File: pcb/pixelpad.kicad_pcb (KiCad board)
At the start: 2 copper layers, 16 parts, among them J1 OLED Display, SW1 SW_Push_45deg, SW2 SW_Push_45deg, SW3 RotaryEncoder_Switch, SW4 SW_Push_45deg, SW5 SW_Push_45deg, SW6 SW_Push_45deg, U1 MOUDLE-SEEEDUINO-XIAO

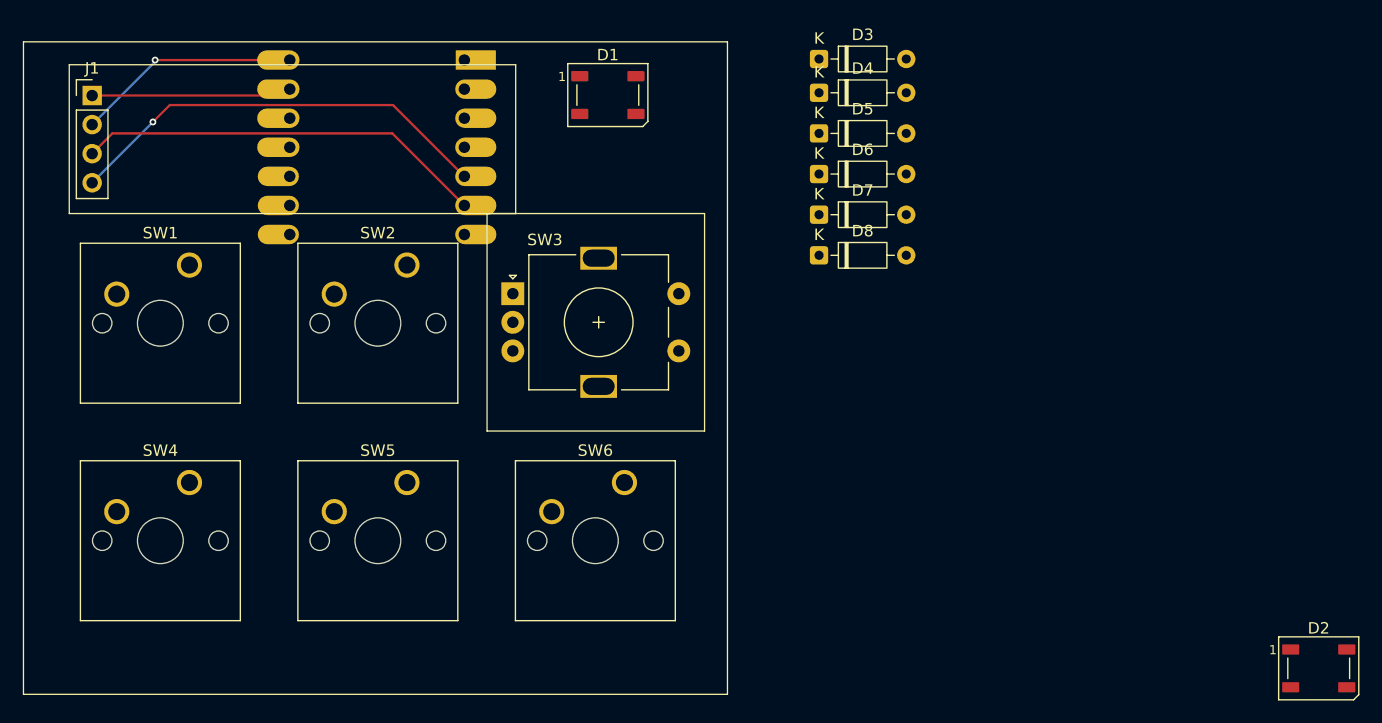
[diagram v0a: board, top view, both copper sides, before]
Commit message: Reordering pins so it's easier to route
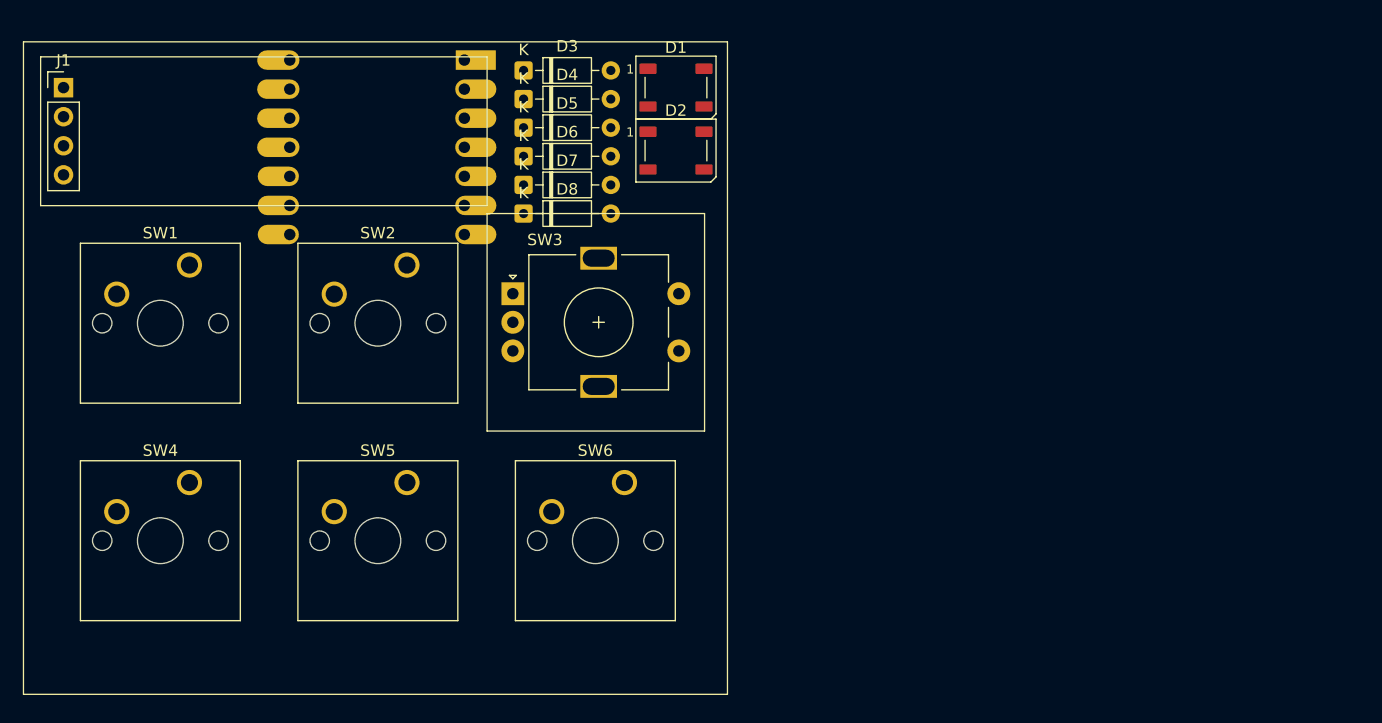
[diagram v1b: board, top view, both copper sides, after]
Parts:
- moved D2 72.1 mm to (112.5, 44.0)
- moved D8 26.1 mm to (99.2, 49.5)
- moved D7 25.9 mm to (99.2, 47.0)
- moved D6 25.9 mm to (99.2, 44.5)
- moved D3 25.8 mm to (99.2, 37.0)
- moved D4 25.8 mm to (99.2, 39.5)
- moved D5 25.8 mm to (99.2, 42.0)
- moved D1 5.99 mm to (112.5, 38.5)
- moved J1 2.59 mm to (59.0, 38.5)
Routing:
- net SDA: track 37.9 -> 0.00 mm, vias 1 -> 0
- net SCL: track 35.9 -> 0.00 mm
- net VCC: track 19.7 -> 0.00 mm, vias 1 -> 0
- net GND: track 17.5 -> 0.00 mm
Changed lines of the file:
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@@
 	(footprint "LED_SMD:LED_WS2812B_PLCC4_5.0x5.0mm_P3.2mm"
 		(layer "F.Cu")
-		(at 168.65 89.23)
+		(at 112.5 44)
 		(descr "5.0mm x 5.0mm Addressable RGB LED NeoPixel, https://cdn-shop.adafruit.com/datasheets/WS2812B.pdf")
 		(tags "LED RGB NeoPixel PLCC-4 5050")
@@
 	(footprint "Diode_THT:D_DO-35_SOD27_P7.62mm_Horizontal"
 		(layer "F.Cu")
-		(at 125 38.95)
+		(at 99.19 39.5)
 		(descr "Diode, DO-35_SOD27 series, Axial, Horizontal, pin pitch=7.62mm, length*diameter=4*2mm^2, http://www.diodes.com/_files/packages/DO-35.pdf")
 		(tags "Diode DO-35_SOD27 series Axial Horizontal pin pitch 7.62mm  length 4mm diameter 2mm")
@@
 		)
 		(property "Value" "1N914"
-			(at 3.81 2.12 0)
+			(at 3.81 -2.53 0)
 			(layer "F.Fab")
 			(effects
@@
 	(footprint "Diode_THT:D_DO-35_SOD27_P7.62mm_Horizontal"
 		(layer "F.Cu")
-		(at 125 46.05)
+		(at 99.19 44.5)
 		(descr "Diode, DO-35_SOD27 series, Axial, Horizontal, pin pitch=7.62mm, length*diameter=4*2mm^2, http://www.diodes.com/_files/packages/DO-35.pdf")
 		(tags "Diode DO-35_SOD27 series Axial Horizontal pin pitch 7.62mm  length 4mm diameter 2mm")
@@
 	(footprint "LED_SMD:LED_WS2812B_PLCC4_5.0x5.0mm_P3.2mm"
 		(layer "F.Cu")
-		(at 106.55 39.15)
+		(at 112.5 38.5)
 		(descr "5.0mm x 5.0mm Addressable RGB LED NeoPixel, https://cdn-shop.adafruit.com/datasheets/WS2812B.pdf")
 		(tags "LED RGB NeoPixel PLCC-4 5050")
@@
 	(footprint "Diode_THT:D_DO-35_SOD27_P7.62mm_Horizontal"
 		(layer "F.Cu")
-		(at 125 42.5)
+		(at 99.19 42)
 		(descr "Diode, DO-35_SOD27 series, Axial, Horizontal, pin pitch=7.62mm, length*diameter=4*2mm^2, http://www.diodes.com/_files/packages/DO-35.pdf")
 		(tags "Diode DO-35_SOD27 series Axial Horizontal pin pitch 7.62mm  length 4mm diameter 2mm")
@@
 	(footprint "Connector_PinHeader_2.54mm:PinHeader_1x04_P2.54mm_Vertical"
 		(layer "F.Cu")
-		(at 61.5 39.19)
+		(at 59 38.5)
 		(descr "Through hole straight pin header, 1x04, 2.54mm pitch, single row")
 		(tags "Through hole pin header THT 1x04 2.54mm single row")
@@
 	(footprint "Diode_THT:D_DO-35_SOD27_P7.62mm_Horizontal"
 		(layer "F.Cu")
-		(at 125 49.6)
+		(at 99.19 47)
 		(descr "Diode, DO-35_SOD27 series, Axial, Horizontal, pin pitch=7.62mm, length*diameter=4*2mm^2, http://www.diodes.com/_files/packages/DO-35.pdf")
 		(tags "Diode DO-35_SOD27 series Axial Horizontal pin pitch 7.62mm  length 4mm diameter 2mm")
@@
 	(footprint "Diode_THT:D_DO-35_SOD27_P7.62mm_Horizontal"
 		(layer "F.Cu")
-		(at 125 36)
+		(at 99.19 37)
 		(descr "Diode, DO-35_SOD27 series, Axial, Horizontal, pin pitch=7.62mm, length*diameter=4*2mm^2, http://www.diodes.com/_files/packages/DO-35.pdf")
 		(tags "Diode DO-35_SOD27 series Axial Horizontal pin pitch 7.62mm  length 4mm diameter 2mm")
@@
 	(footprint "Diode_THT:D_DO-35_SOD27_P7.62mm_Horizontal"
 		(layer "F.Cu")
-		(at 125 53.15)
+		(at 99.19 49.5)
 		(descr "Diode, DO-35_SOD27 series, Axial, Horizontal, pin pitch=7.62mm, length*diameter=4*2mm^2, http://www.diodes.com/_files/packages/DO-35.pdf")
 		(tags "Diode DO-35_SOD27 series Axial Horizontal pin pitch 7.62mm  length 4mm diameter 2mm")
@@
 	)
 	(gr_rect
-		(start 59.5 36.5)
-		(end 98.5 49.5)
+		(start 57 35.81)
+		(end 96 48.81)
 		(stroke
 			(width 0.1)
@@
 		(layer "F.SilkS")
 	)
-	(segment
-		(start 67 36.092015)
-		(end 78.7645 36.092015)
-		(width 0.2)
-		(layer "F.Cu")
-		(net "VCC")
-	)
-	(via
-		(at 67 36.092015)
-		(size 0.6)
-		(drill 0.3)
-		(layers "F.Cu" "B.Cu")
-		(net "VCC")
-	)
-	(segment
-		(start 67 36.23)
-		(end 61.5 41.73)
-		(width 0.2)
-		(layer "B.Cu")
-		(net "VCC")
-	)
-	(segment
-		(start 67 36.092015)
-		(end 67 36.23)
-		(width 0.2)
-		(layer "B.Cu")
-		(net "VCC")
-	)
-	(segment
-		(start 78.206515 39.19)
-		(end 78.7645 38.632015)
-		(width 0.2)
-		(layer "F.Cu")
-		(net "GND")
-	)
-	(segment
-		(start 61.5 39.19)
-		(end 78.206515 39.19)
-		(width 0.2)
-		(layer "F.Cu")
-		(net "GND")
-	)
-	(segment
-		(start 63.27 42.5)
-		(end 61.5 44.27)
-		(width 0.2)
-		(layer "F.Cu")
-		(net "SCL")
-	)
-	(segment
-		(start 87.722485 42.5)
-		(end 63.27 42.5)
-		(width 0.2)
-		(layer "F.Cu")
-		(net "SCL")
-	)
-	(segment
-		(start 94.0145 48.792015)
-		(end 87.722485 42.5)
-		(width 0.2)
-		(layer "F.Cu")
-		(net "SCL")
-	)
-	(segment
-		(start 66.81 41.5)
-		(end 68.287985 40.022015)
-		(width 0.2)
-		(layer "F.Cu")
-		(net "SDA")
-	)
-	(segment
-		(start 68.287985 40.022015)
-		(end 87.7845 40.022015)
-		(width 0.2)
-		(layer "F.Cu")
-		(net "SDA")
-	)
-	(segment
-		(start 87.7845 40.022015)
-		(end 94.0145 46.252015)
-		(width 0.2)
-		(layer "F.Cu")
-		(net "SDA")
-	)
-	(via
-		(at 66.81 41.5)
-		(size 0.6)
-		(drill 0.3)
-		(layers "F.Cu" "B.Cu")
-		(net "SDA")
-	)
-	(segment
-		(start 66.81 41.5)
-		(end 61.5 46.81)
-		(width 0.2)
-		(layer "B.Cu")
-		(net "SDA")
-	)
 	(group ""

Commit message: Ran DRC and no more errors
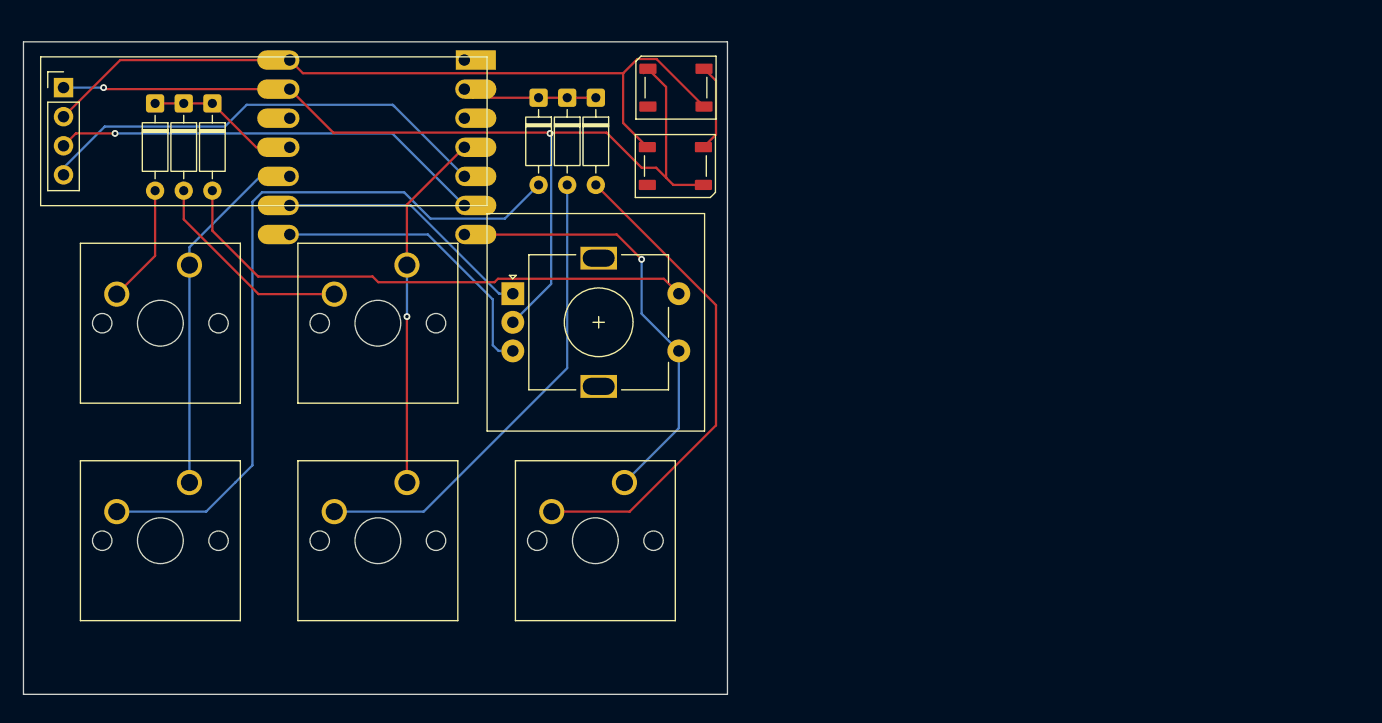
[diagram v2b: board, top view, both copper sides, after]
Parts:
- moved D3 32.3 mm to (67.0, 39.9), turned to -90 degrees
- moved D4 29.7 mm to (69.5, 39.9), turned to -90 degrees
- moved D5 27.3 mm to (72.0, 39.9), turned to -90 degrees
- moved D8 11.9 mm to (105.5, 39.4), turned to -90 degrees
- moved D7 8.52 mm to (103.0, 39.4), turned to -90 degrees
- moved D6 5.28 mm to (100.5, 39.4), turned to -90 degrees
- moved D2 1.35 mm to (112.5, 45.4)
- turned D1 to 180 degrees
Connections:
- U1 pad 1: COL0 -> unconnected-(U1-PA02_A0_D0-Pad1)
- U1 pad 10: COL2 -> COL0
- U1 pad 11: COL1 -> ROW0
- U1 pad 2: unconnected-(U1-PA4_A1_D1-Pad2) -> ROW1
- U1 pad 3: ROW1 -> unconnected-(U1-PA10_A2_D2-Pad3)
- U1 pad 4: ROW0 -> COL1
- U1 pad 7: unconnected-(U1-PB08_A6_D6_TX-Pad7) -> COL2
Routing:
- net GND: track 0.00 -> 88.2 mm, vias 0 -> 2
- net VCC: track 0.00 -> 68.0 mm
- net Net-(D6-A): track 0.00 -> 64.1 mm
- net EC11SWA: track 0.00 -> 46.8 mm
- net Net-(D8-A): track 0.00 -> 42.8 mm
- net Net-(D7-A): track 0.00 -> 41.5 mm
- net SDA: track 0.00 -> 40.6 mm
- net COL2: track 0.00 -> 39.2 mm, vias 0 -> 1
- net SCL: track 0.00 -> 38.1 mm, vias 0 -> 1
- net COL0: track 0.00 -> 31.9 mm
- net COL1: track 0.00 -> 31.4 mm, vias 0 -> 1
- net EC11B: track 0.00 -> 26.0 mm
- net EC11A: track 0.00 -> 22.7 mm
- net Net-(D4-A): track 0.00 -> 18.4 mm
- net ROW0: track 0.00 -> 13.4 mm
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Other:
- board outline added: 61.5 x 57 mm

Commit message: Trying to add custom silkscreen
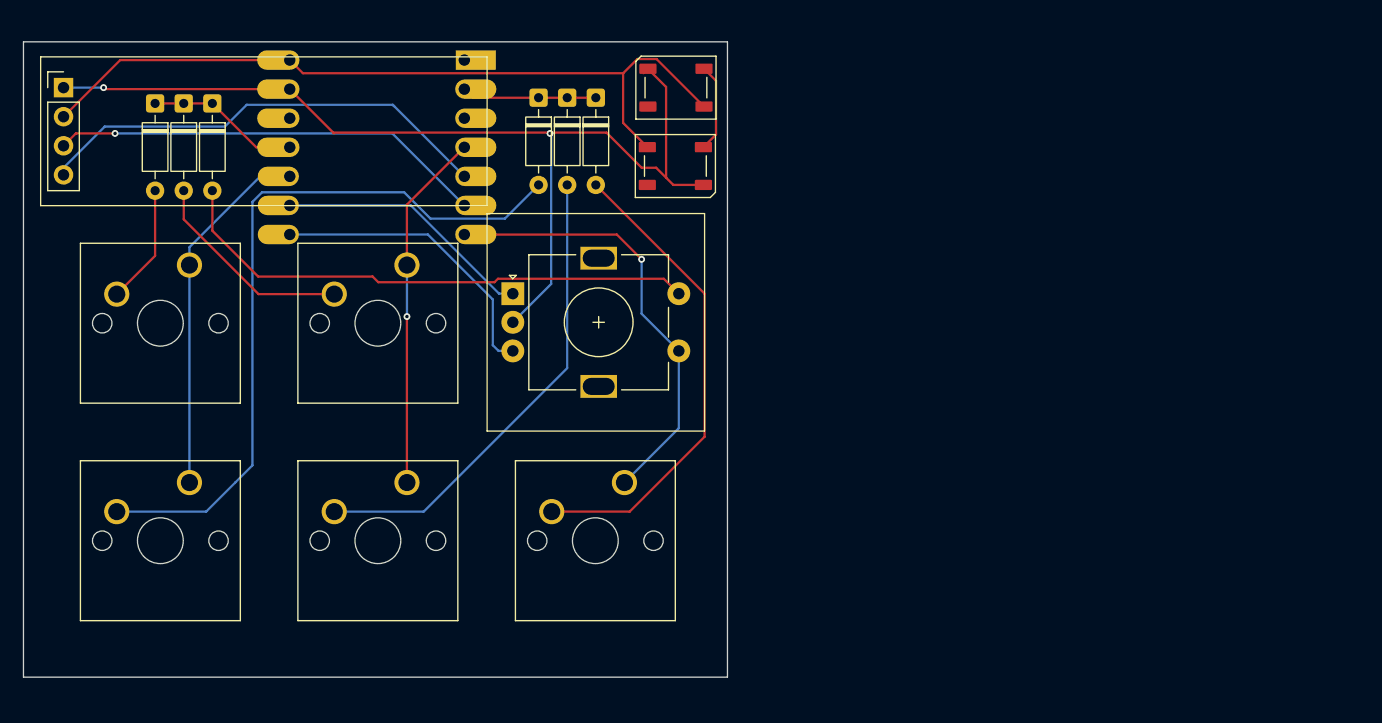
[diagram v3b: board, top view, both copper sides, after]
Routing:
- net Net-(D8-A): track 42.8 -> 42.0 mm
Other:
- board size 61.5 x 57 mm -> 61.5 x 55.5 mm
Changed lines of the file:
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@@
 	(gr_rect
 		(start 55.5 34.5)
-		(end 117 91.5)
+		(end 117 90)
 		(stroke
 			(width 0.05)
@@
 	)
 	(segment
-		(start 116 57.5)
-		(end 116 68)
+		(start 105.5 47)
+		(end 115 56.5)
+		(width 0.2)
+		(layer "F.Cu")
+		(net "Net-(D8-A)")
+	)
+	(segment
+		(start 115 69)
+		(end 108.46 75.54)
+		(width 0.2)
+		(layer "F.Cu")
+		(net "Net-(D8-A)")
+	)
+	(segment
+		(start 115 56.5)
+		(end 115 69)
 		(width 0.2)
 		(layer "F.Cu")
@@
 	)
 	(segment
-		(start 105.5 47)
-		(end 116 57.5)
-		(width 0.2)
-		(layer "F.Cu")
-		(net "Net-(D8-A)")
-	)
-	(segment
-		(start 116 68)
-		(end 108.46 75.54)
-		(width 0.2)
-		(layer "F.Cu")
-		(net "Net-(D8-A)")
+		(start 89.342015 48.792015)
+		(end 97.05 56.5)
+		(width 0.2)
+		(layer "B.Cu")
+		(net "EC11A")
+	)
+	(segment
+		(start 78.7645 48.792015)
+		(end 89.342015 48.792015)
+		(width 0.2)
+		(layer "B.Cu")
+		(net "EC11A")
+	)
+	(segment
+		(start 97.05 56.5)
+		(end 98.25 56.5)
+		(width 0.2)
+		(layer "B.Cu")
+		(net "EC11A")
 	)
 	(segment
@@
 		(net "EC11B")
 	)
-	(segment
-		(start 89.342015 48.792015)
-		(end 97.05 56.5)
-		(width 0.2)
-		(layer "B.Cu")
-		(net "EC11A")
-	)
-	(segment
-		(start 78.7645 48.792015)
-		(end 89.342015 48.792015)
-		(width 0.2)
-		(layer "B.Cu")
-		(net "EC11A")
-	)
-	(segment
-		(start 97.05 56.5)
-		(end 98.25 56.5)
-		(width 0.2)
-		(layer "B.Cu")
-		(net "EC11A")
-	)
 	(embedded_fonts no)

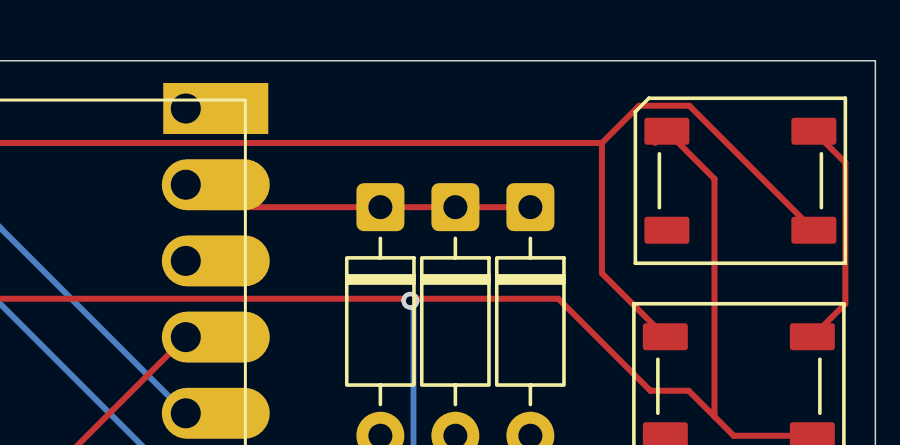
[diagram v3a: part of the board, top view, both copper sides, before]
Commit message: Added the silkscreen art properly
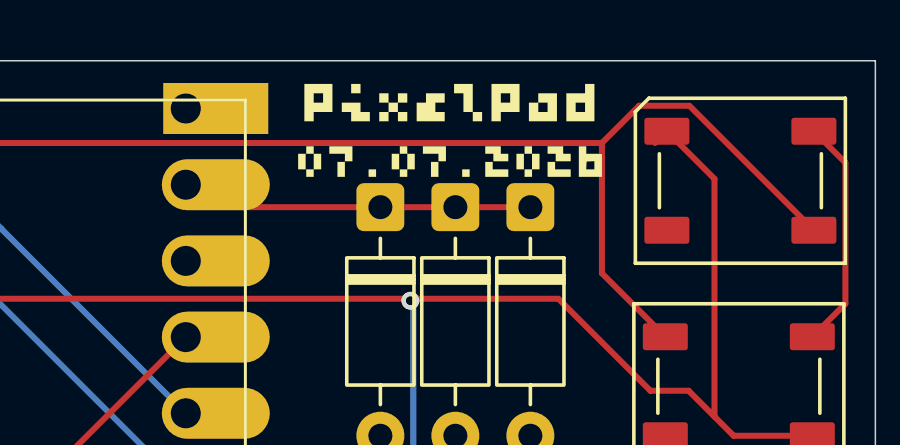
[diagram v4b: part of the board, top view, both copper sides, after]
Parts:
- added G***: LOGO, silkscreen:silkscreen, F.Cu at (103.0, 37.0)
